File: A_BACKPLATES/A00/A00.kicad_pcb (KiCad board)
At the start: 2 copper layers, 75 x 49 mm, 39 parts, among them J0 Conn_01x01_Male, J1 Conn_01x01_Male, J2 Conn_01x01_Male, J3 Conn_01x01_Male

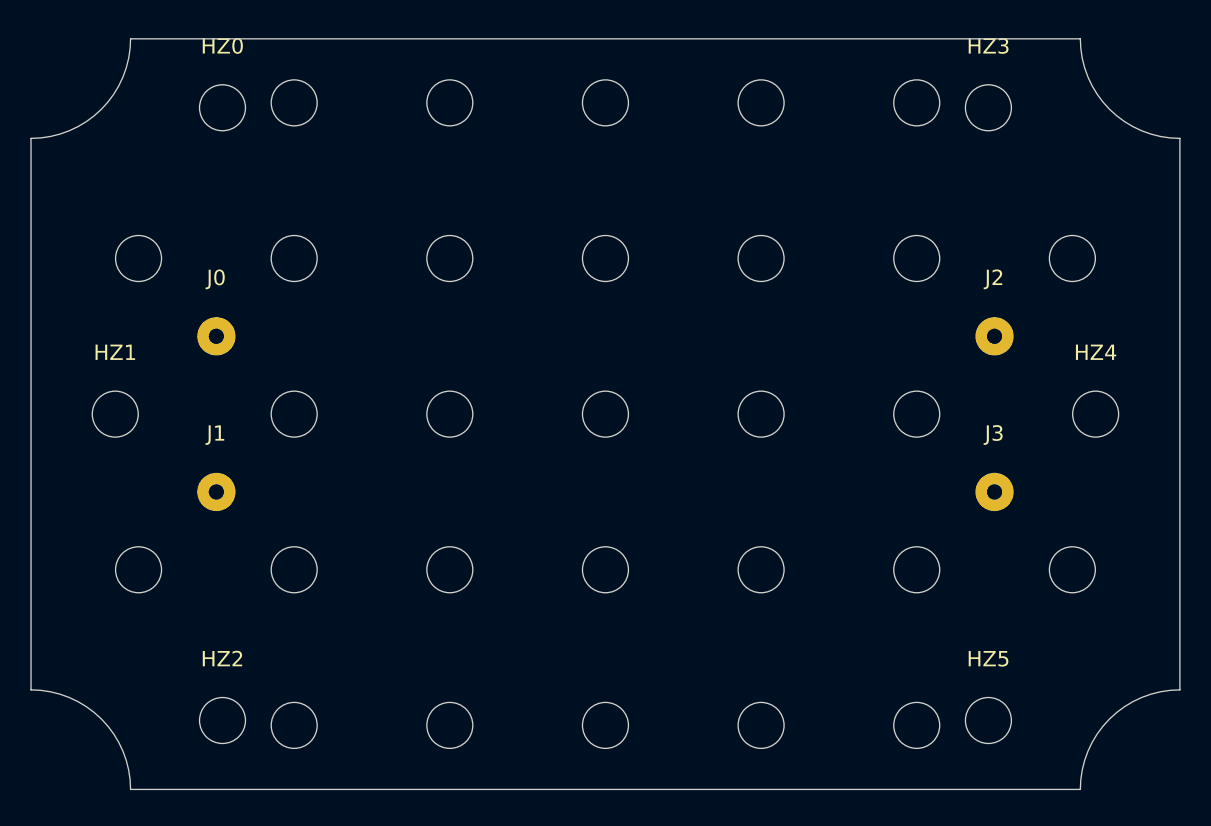
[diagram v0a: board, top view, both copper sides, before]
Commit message: added gerbers single and panel
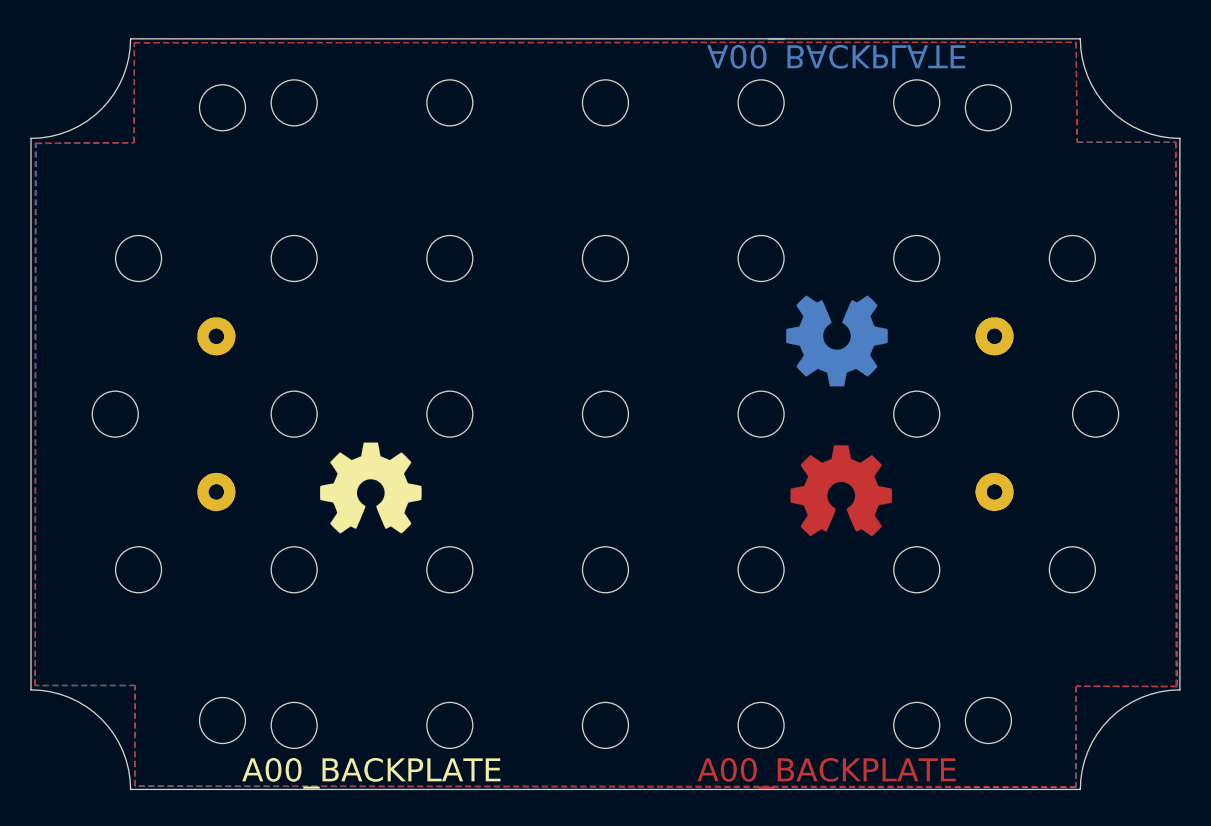
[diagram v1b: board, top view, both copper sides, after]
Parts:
- added REF**: OSHW-Symbol_6.7x6mm_Copper, Symbol:OSHW-Symbol_6.7x6mm_Copper, B.Cu at (152.6, 119.7)
- added REF**: OSHW-Symbol_6.7x6mm_SilkScreen, Symbol:OSHW-Symbol_6.7x6mm_SilkScreen, B.Cu at (122.2, 119.7)
- added REF**: OSHW-Symbol_6.7x6mm_Copper, Symbol:OSHW-Symbol_6.7x6mm_Copper, F.Cu at (152.9, 129.5)
- added REF**: OSHW-Symbol_6.7x6mm_SilkScreen, Symbol:OSHW-Symbol_6.7x6mm_SilkScreen, F.Cu at (122.2, 129.3)
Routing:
- added copper zone on B.Cu, net Net-(J0-Pad1)
- added copper zone on F.Cu, net Net-(J0-Pad1)
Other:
- board text added: "A00_BACKPLATE"
